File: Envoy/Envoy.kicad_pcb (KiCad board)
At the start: 2 copper layers, 95.4 x 95.4 mm, 57 parts

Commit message: Move standoff and bumper positioning to make the backplate work easier
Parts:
- moved H1 4.75 mm to (130.5, 64.3)
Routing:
- net col1: track 146.9 -> 148.8 mm
- net col0: track 167.3 -> 168.5 mm
- net GND: vias 35 -> 36
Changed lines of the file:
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@@
   )
   (footprint "Envoy:ClearanceHole_3.7mm" (layer "F.Cu")
-    (at 135.287 64.29375)
+    (at 130.537 64.29375)
     (descr "Mounting Hole 3.7mm, no annular")
     (tags "mounting hole 3.7mm no annular")
@@
   (via (at 151.3 56.9) (size 0.8) (drill 0.4) (layers "F.Cu" "B.Cu") (free) (net 31))
   (via (at 113.2 56.9) (size 0.8) (drill 0.4) (layers "F.Cu" "B.Cu") (free) (net 31))
+  (via (at 146.4 62.4) (size 0.8) (drill 0.4) (layers "F.Cu" "B.Cu") (free) (net 31))
   (via (at 174.5 78.1) (size 0.8) (drill 0.4) (layers "F.Cu" "B.Cu") (free) (net 31))
   (via (at 143.4 76) (size 0.8) (drill 0.4) (layers "F.Cu" "B.Cu") (free) (net 31))
@@
   (via (at 173 105.9) (size 0.8) (drill 0.4) (layers "F.Cu" "B.Cu") (free) (net 31))
   (via (at 101.2 80.8) (size 0.8) (drill 0.4) (layers "F.Cu" "B.Cu") (free) (net 31))
-  (via (at 101.2 61.8) (size 0.8) (drill 0.4) (layers "F.Cu" "B.Cu") (free) (net 31))
+  (via (at 101.2 67.2) (size 0.8) (drill 0.4) (layers "F.Cu" "B.Cu") (free) (net 31))
   (via (at 132.4 95.1) (size 0.8) (drill 0.4) (layers "F.Cu" "B.Cu") (free) (net 31))
   (via (at 151.5 133.1) (size 0.8) (drill 0.4) (layers "F.Cu" "B.Cu") (free) (net 31))
@@
   (segment (start 186.055 51.689) (end 193.3489 51.689) (width 0.25) (layer "F.Cu") (net 32))
   (segment (start 183.2375 47.26875) (end 183.2375 48.8715) (width 0.25) (layer "F.Cu") (net 32))
-  (segment (start 176.75 65.132182) (end 175.181222 66.70096) (width 0.25) (layer "F.Cu") (net 33))
-  (segment (start 102.861098 66.17594) (end 102.489038 66.548) (width 0.25) (layer "F.Cu") (net 33))
-  (segment (start 132.786198 66.65048) (end 132.311658 66.17594) (width 0.25) (layer "F.Cu") (net 33))
-  (segment (start 175.181222 66.70096) (end 156.20096 66.70096) (width 0.25) (layer "F.Cu") (net 33))
-  (segment (start 132.311658 66.17594) (end 102.861098 66.17594) (width 0.25) (layer "F.Cu") (net 33))
-  (segment (start 155.40096 65.90096) (end 141.280104 65.90096) (width 0.25) (layer "F.Cu") (net 33))
-  (segment (start 156.20096 66.70096) (end 155.40096 65.90096) (width 0.25) (layer "F.Cu") (net 33))
-  (segment (start 140.530584 66.65048) (end 132.786198 66.65048) (width 0.25) (layer "F.Cu") (net 33))
-  (segment (start 141.280104 65.90096) (end 140.530584 66.65048) (width 0.25) (layer "F.Cu") (net 33))
-  (segment (start 178.1289 61.849) (end 176.75 63.2279) (width 0.25) (layer "F.Cu") (net 33))
-  (segment (start 176.75 63.2279) (end 176.75 65.132182) (width 0.25) (layer "F.Cu") (net 33))
-  (via (at 102.489038 66.548) (size 0.8) (drill 0.4) (layers "F.Cu" "B.Cu") (net 33))
+  (segment (start 153.79375 64.29375) (end 156.20096 66.70096) (width 0.25) (layer "F.Cu") (net 33))
+  (segment (start 121.664282 63) (end 122.864283 61.8) (width 0.25) (layer "F.Cu") (net 33))
+  (segment (start 173.27694 66.70096) (end 178.1289 61.849) (width 0.25) (layer "F.Cu") (net 33))
+  (segment (start 102.4525 61.8475) (end 103.605 63) (width 0.25) (layer "F.Cu") (net 33))
+  (segment (start 134.529468 64.29375) (end 153.79375 64.29375) (width 0.25) (layer "F.Cu") (net 33))
+  (segment (start 131.686198 61.45048) (end 134.529468 64.29375) (width 0.25) (layer "F.Cu") (net 33))
+  (segment (start 122.864283 61.8) (end 125.739283 61.8) (width 0.25) (layer "F.Cu") (net 33))
+  (segment (start 125.739283 61.8) (end 126.088803 61.45048) (width 0.25) (layer "F.Cu") (net 33))
+  (segment (start 103.605 63) (end 121.664282 63) (width 0.25) (layer "F.Cu") (net 33))
+  (segment (start 126.088803 61.45048) (end 131.686198 61.45048) (width 0.25) (layer "F.Cu") (net 33))
+  (segment (start 156.20096 66.70096) (end 173.27694 66.70096) (width 0.25) (layer "F.Cu") (net 33))
+  (via (at 102.4525 61.8475) (size 0.8) (drill 0.4) (layers "F.Cu" "B.Cu") (net 33))
   (segment (start 102.4525 90.32875) (end 102.4525 109.37875) (width 0.25) (layer "B.Cu") (net 33))
   (segment (start 108.87075 128.42875) (end 106.68 126.238) (width 0.25) (layer "B.Cu") (net 33))
   (segment (start 106.68 126.238) (end 104.64325 126.238) (width 0.25) (layer "B.Cu") (net 33))
-  (segment (start 102.4525 52.22875) (end 102.4525 90.32875) (width 0.25) (layer "B.Cu") (net 33))
+  (segment (start 102.4525 52.22875) (end 102.4525 61.8475) (width 0.25) (layer "B.Cu") (net 33))
   (segment (start 111.9775 128.42875) (end 108.87075 128.42875) (width 0.25) (layer "B.Cu") (net 33))
+  (segment (start 102.4525 61.8475) (end 102.4525 90.32875) (width 0.25) (layer "B.Cu") (net 33))
   (segment (start 104.64325 126.238) (end 102.4525 128.42875) (width 0.25) (layer "B.Cu") (net 33))
   (segment (start 102.4525 109.37875) (end 102.4525 128.42875) (width 0.25) (layer "B.Cu") (net 33))
@@
   (segment (start 189.781 64.6) (end 191.9 62.481) (width 0.25) (layer "F.Cu") (net 34))
   (segment (start 188.87915 66.31875) (end 193.3489 61.849) (width 0.25) (layer "F.Cu") (net 35))
-  (segment (start 122.07454 66.62546) (end 132.12546 66.62546) (width 0.25) (layer "F.Cu") (net 36))
+  (segment (start 121.5 63.8) (end 123.05048 62.24952) (width 0.25) (layer "F.Cu") (net 36))
+  (segment (start 134.34327 64.74327) (end 153.607552 64.74327) (width 0.25) (layer "F.Cu") (net 36))
+  (segment (start 153.607552 64.74327) (end 156.014762 67.15048) (width 0.25) (layer "F.Cu") (net 36))
+  (segment (start 131.5 61.9) (end 134.34327 64.74327) (width 0.25) (layer "F.Cu") (net 36))
   (segment (start 156.014762 67.15048) (end 175.36742 67.15048) (width 0.25) (layer "F.Cu") (net 36))
-  (segment (start 121.5 67.2) (end 122.07454 66.62546) (width 0.25) (layer "F.Cu") (net 36))
-  (segment (start 140.716782 67.1) (end 141.466302 66.35048) (width 0.25) (layer "F.Cu") (net 36))
   (segment (start 175.36742 67.15048) (end 178.1289 64.389) (width 0.25) (layer "F.Cu") (net 36))
-  (segment (start 141.466302 66.35048) (end 155.214762 66.35048) (width 0.25) (layer "F.Cu") (net 36))
-  (segment (start 132.12546 66.62546) (end 132.6 67.1) (width 0.25) (layer "F.Cu") (net 36))
-  (segment (start 132.6 67.1) (end 140.716782 67.1) (width 0.25) (layer "F.Cu") (net 36))
-  (segment (start 155.214762 66.35048) (end 156.014762 67.15048) (width 0.25) (layer "F.Cu") (net 36))
-  (via (at 121.5 67.2) (size 0.8) (drill 0.4) (layers "F.Cu" "B.Cu") (net 36))
+  (segment (start 125.92548 62.24952) (end 126.275 61.9) (width 0.25) (layer "F.Cu") (net 36))
+  (segment (start 126.275 61.9) (end 131.5 61.9) (width 0.25) (layer "F.Cu") (net 36))
+  (segment (start 123.05048 62.24952) (end 125.92548 62.24952) (width 0.25) (layer "F.Cu") (net 36))
+  (via (at 121.5 63.8) (size 0.8) (drill 0.4) (layers "F.Cu" "B.Cu") (net 36))
   (segment (start 122.7455 136.04875) (end 125.857 132.93725) (width 0.25) (layer "B.Cu") (net 36))
   (segment (start 121.5025 111.689752) (end 121.5025 109.37875) (width 0.25) (layer "B.Cu") (net 36))

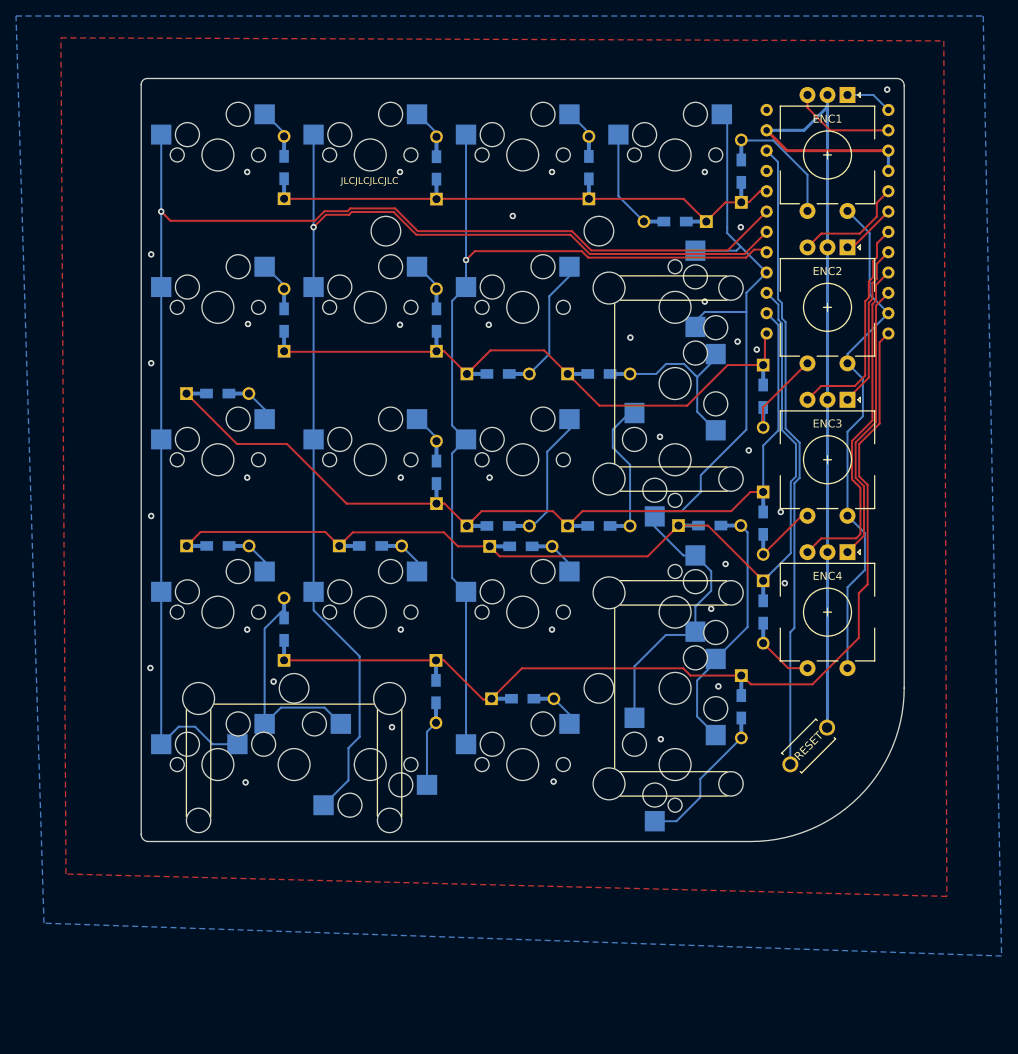
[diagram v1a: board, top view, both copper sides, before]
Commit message: More tweaks to the switchplate cutouts, make switchplate float instead of the PCB, move diodes to give more space to stabs
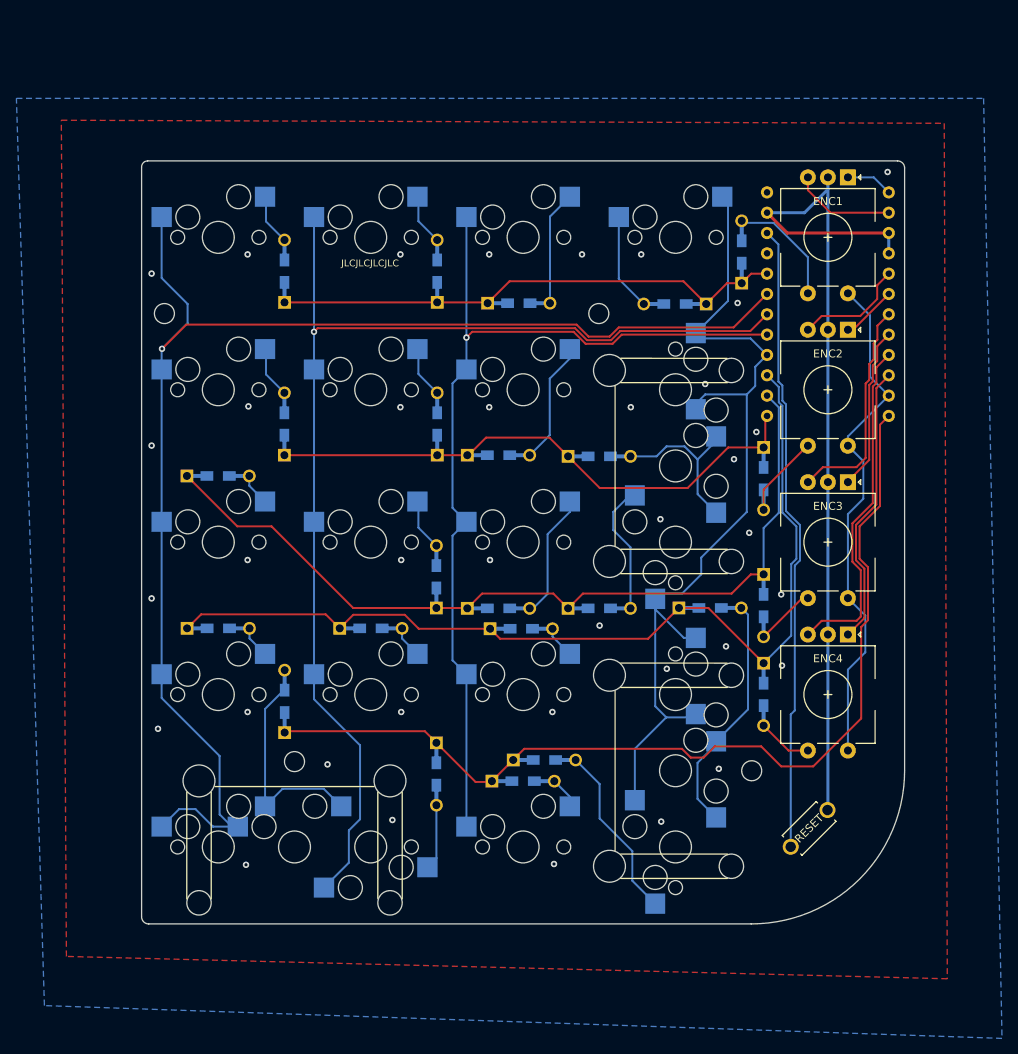
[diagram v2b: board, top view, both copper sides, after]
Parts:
- H1, H2, H3, H4: footprint Envoy:ClearanceHole_3.7mm -> MountingHole:MountingHole_2.5mm
- RESET1: footprint Envoy:Reset_Jumper_Points -> kbd:ResetSW
- moved H1 29.5 mm to (102.9, 74.6)
- moved D20 25.5 mm to (150.4, 130.4), turned to 180 degrees
- moved H4 21.7 mm to (176.3, 131.7)
- moved D3 19.1 mm to (147.2, 73.3), turned to 180 degrees
- moved D10 13.1 mm to (136.9, 107.5)
- moved D6 13.0 mm to (137.0, 88.4)
- moved D5 13.0 mm to (117.9, 88.4)
- moved D1 13.0 mm to (117.9, 69.3)
- moved D2 12.9 mm to (137.0, 69.3)
- moved D4 10.3 mm to (166.7, 73.4)
- moved D15 10.3 mm to (147.5, 114.0)
- moved D18 10.3 mm to (136.9, 132.2)
- moved ENC2 10.3 mm to (185.8, 84.1)
- moved MX16-2u1 10.3 mm to (166.7, 131.7)
- moved MX17 10.3 mm to (109.6, 141.3)
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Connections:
- ProMicro1 pad 24: Net-(U1-Pad24) -> unconnected-(ProMicro1-Pad24)
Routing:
- net Net-(D3-Pad2): track 3.72 -> 14.3 mm
- net col0: track 168.5 -> 174.3 mm
- net Net-(D20-Pad2): track 16.5 -> 22.1 mm
- net col3: track 109.4 -> 113.5 mm
- net Net-(D10-Pad2): track 3.71 -> 6.44 mm
- net Net-(D6-Pad2): track 3.72 -> 6.43 mm
- net Net-(D5-Pad2): track 3.72 -> 6.41 mm
- net Net-(D1-Pad2): track 3.71 -> 6.37 mm
- net Net-(D2-Pad2): track 3.76 -> 6.38 mm
- net row4: track 119.1 -> 121.2 mm
- net col1: track 148.8 -> 146.8 mm
- net row1: track 71.3 -> 69.6 mm
- net row0: track 63.1 -> 64.2 mm
- net GND: vias 36 -> 37

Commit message: Moved most diodes to horizontal layout to enable better access for soldering hotswap sockets
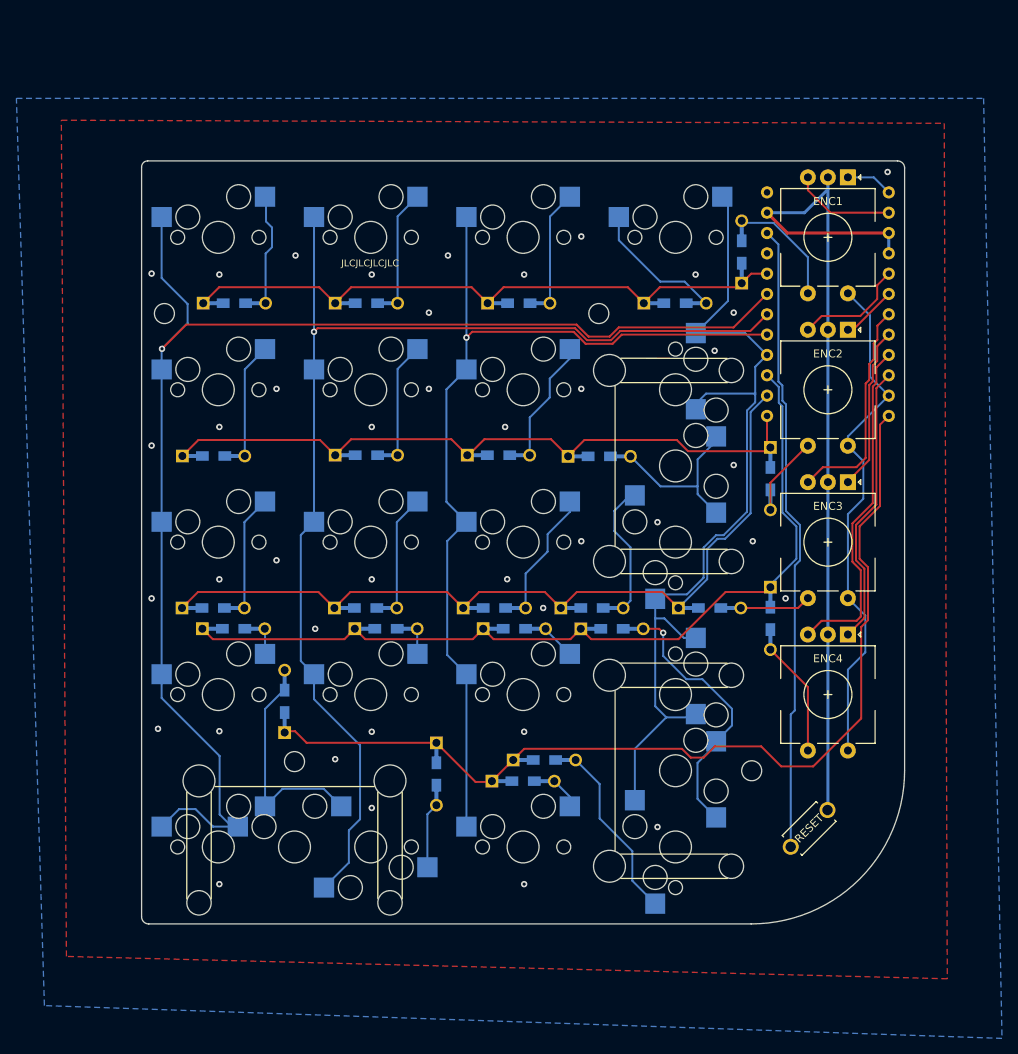
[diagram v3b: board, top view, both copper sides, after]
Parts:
- moved D9 16.5 mm to (109.0, 111.4)
- moved D16 12.5 mm to (158.8, 114.0)
- moved D2 9.71 mm to (128.1, 73.3), turned to 180 degrees
- moved D5 9.71 mm to (109.0, 92.4), turned to 180 degrees
- moved D10 9.67 mm to (128.0, 111.4), turned to 180 degrees
- moved D6 9.67 mm to (128.1, 92.3), turned to 180 degrees
- moved D24 9.54 mm to (178.6, 112.7)
- moved D1 7.43 mm to (111.6, 73.3), turned to 180 degrees
- moved D23 6.76 mm to (171.0, 111.4), turned to 180 degrees
- moved D13 1.91 mm to (111.5, 114.0)
- moved D14 1.89 mm to (130.6, 114.0)
- moved D12 0.91 mm to (156.3, 111.4)
- moved D15 0.86 mm to (146.6, 114.0)
- moved D22 0.85 mm to (178.6, 95.2)
- moved D11 0.52 mm to (144.1, 111.4)
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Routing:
- net row1: track 69.6 -> 84.2 mm
- net row0: track 64.2 -> 77.0 mm
- net row3: track 119.1 -> 106.8 mm
- net Net-(D9-Pad2): track 4.01 -> 14.4 mm
- net Net-(D5-Pad2): track 6.41 -> 14.4 mm
- net Net-(D2-Pad2): track 6.38 -> 14.4 mm
- net Net-(D10-Pad2): track 6.44 -> 14.4 mm
- net Net-(D6-Pad2): track 6.43 -> 14.3 mm
- net Net-(D24-Pad2): track 6.83 -> 14.6 mm
- net Net-(D1-Pad2): track 6.37 -> 14.0 mm
- net row2: track 106.0 -> 100.4 mm
- net Net-(D4-Pad2): track 12.2 -> 17.1 mm
- net Net-(D16-Pad2): track 30.1 -> 33.3 mm, vias 0 -> 1
- net Net-(D23-Pad2): track 7.43 -> 8.90 mm
- net col1: track 146.8 -> 148.2 mm
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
